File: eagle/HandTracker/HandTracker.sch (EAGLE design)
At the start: 9 parts, among them J1 ZX62-AB-5PA(31), U1 LSM9DS1TR, U2 MAX11629EEE+21-0055_E16+5_MXM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, U3 ATMEGA16U2-MU32M1-A_ATM-M

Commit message: continued making connections
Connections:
- new net CSA: U2.!CS
- new net CSAG: U1.CS_A/G
- new net CSM: U1.CS_M
- new net MISO: U$1.14, U1.SDO_A/G, U1.SDO_M, U2.DOUT
- new net MOSI: U$1.15, U1.SDA/SDI/SDO, U2.DIN
- new net SCLK: U$1.7, U1.SCL/SPC, U2.SCLK
- net GND: now also U1.GND, U1.GND_2, U1.RES, U1.RES_2, U1.RES_3, U1.RES_4, U1.RES_5, U2.GND
- net VCC: now also U1.VDD, U1.VDDIO, U1.VDDIO_2, U1.VDD_2, U2.REF, U2.VDD
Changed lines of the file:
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@@
 <part name="GND4" library="supply1" library_urn="urn:adsk.eagle:library:371" deviceset="GND" device=""/>
 <part name="P+3" library="supply1" library_urn="urn:adsk.eagle:library:371" deviceset="VCC" device=""/>
+<part name="P+4" library="supply1" library_urn="urn:adsk.eagle:library:371" deviceset="VCC" device=""/>
+<part name="GND5" library="supply1" library_urn="urn:adsk.eagle:library:371" deviceset="GND" device=""/>
+<part name="P+5" library="supply1" library_urn="urn:adsk.eagle:library:371" deviceset="VCC" device=""/>
+<part name="P+6" library="supply1" library_urn="urn:adsk.eagle:library:371" deviceset="VCC" device=""/>
+<part name="GND6" library="supply1" library_urn="urn:adsk.eagle:library:371" deviceset="GND" device=""/>
 </parts>
 <sheets>
@@
 <attribute name="VALUE" x="58.42" y="-53.34" size="1.778" layer="96" rot="R90"/>
 </instance>
+<instance part="P+4" gate="VCC" x="119.38" y="76.2" smashed="yes">
+<attribute name="VALUE" x="116.84" y="73.66" size="1.778" layer="96" rot="R90"/>
+</instance>
+<instance part="GND5" gate="1" x="119.38" y="58.42" smashed="yes">
+<attribute name="VALUE" x="116.84" y="55.88" size="1.778" layer="96"/>
+</instance>
+<instance part="P+5" gate="VCC" x="2.54" y="-25.4" smashed="yes">
+<attribute name="VALUE" x="0" y="-27.94" size="1.778" layer="96" rot="R90"/>
+</instance>
+<instance part="P+6" gate="VCC" x="-76.2" y="-27.94" smashed="yes">
+<attribute name="VALUE" x="-78.74" y="-30.48" size="1.778" layer="96" rot="R90"/>
+</instance>
+<instance part="GND6" gate="1" x="2.54" y="-60.96" smashed="yes">
+<attribute name="VALUE" x="0" y="-63.5" size="1.778" layer="96"/>
+</instance>
 </instances>
 <busses>
@@
 <wire x1="58.42" y1="-58.42" x2="58.42" y2="-73.66" width="0.1524" layer="91"/>
 <pinref part="GND4" gate="1" pin="GND"/>
+</segment>
+<segment>
+<pinref part="U2" gate="A" pin="GND"/>
+<wire x1="86.36" y1="66.04" x2="119.38" y2="66.04" width="0.1524" layer="91"/>
+<wire x1="119.38" y1="66.04" x2="119.38" y2="60.96" width="0.1524" layer="91"/>
+<pinref part="GND5" gate="1" pin="GND"/>
+</segment>
+<segment>
+<pinref part="U1" gate="A" pin="GND"/>
+<wire x1="-7.62" y1="-38.1" x2="2.54" y2="-38.1" width="0.1524" layer="91"/>
+<wire x1="2.54" y1="-38.1" x2="2.54" y2="-40.64" width="0.1524" layer="91"/>
+<pinref part="U1" gate="A" pin="GND_2"/>
+<wire x1="-7.62" y1="-40.64" x2="2.54" y2="-40.64" width="0.1524" layer="91"/>
+<junction x="2.54" y="-40.64"/>
+<pinref part="GND6" gate="1" pin="GND"/>
+<wire x1="2.54" y1="-40.64" x2="2.54" y2="-43.18" width="0.1524" layer="91"/>
+<pinref part="U1" gate="A" pin="RES_2"/>
+<wire x1="2.54" y1="-43.18" x2="2.54" y2="-45.72" width="0.1524" layer="91"/>
+<wire x1="2.54" y1="-45.72" x2="2.54" y2="-48.26" width="0.1524" layer="91"/>
+<wire x1="2.54" y1="-48.26" x2="2.54" y2="-50.8" width="0.1524" layer="91"/>
+<wire x1="2.54" y1="-50.8" x2="2.54" y2="-53.34" width="0.1524" layer="91"/>
+<wire x1="2.54" y1="-53.34" x2="2.54" y2="-58.42" width="0.1524" layer="91"/>
+<wire x1="-7.62" y1="-53.34" x2="2.54" y2="-53.34" width="0.1524" layer="91"/>
+<junction x="2.54" y="-53.34"/>
+<pinref part="U1" gate="A" pin="RES_3"/>
+<wire x1="-7.62" y1="-50.8" x2="2.54" y2="-50.8" width="0.1524" layer="91"/>
+<junction x="2.54" y="-50.8"/>
+<pinref part="U1" gate="A" pin="RES_4"/>
+<wire x1="-7.62" y1="-48.26" x2="2.54" y2="-48.26" width="0.1524" layer="91"/>
+<junction x="2.54" y="-48.26"/>
+<pinref part="U1" gate="A" pin="RES_5"/>
+<wire x1="-7.62" y1="-45.72" x2="2.54" y2="-45.72" width="0.1524" layer="91"/>
+<junction x="2.54" y="-45.72"/>
+<pinref part="U1" gate="A" pin="RES"/>
+<wire x1="-7.62" y1="-43.18" x2="2.54" y2="-43.18" width="0.1524" layer="91"/>
+<junction x="2.54" y="-43.18"/>
 </segment>
 </net>
@@
 <wire x1="60.96" y1="-60.96" x2="76.2" y2="-60.96" width="0.1524" layer="91"/>
 </segment>
+<segment>
+<pinref part="U2" gate="A" pin="VDD"/>
+<wire x1="86.36" y1="68.58" x2="93.98" y2="68.58" width="0.1524" layer="91"/>
+<wire x1="93.98" y1="68.58" x2="119.38" y2="68.58" width="0.1524" layer="91"/>
+<wire x1="119.38" y1="68.58" x2="119.38" y2="73.66" width="0.1524" layer="91"/>
+<wire x1="93.98" y1="68.58" x2="93.98" y2="63.5" width="0.1524" layer="91"/>
+<junction x="93.98" y="68.58"/>
+<pinref part="U2" gate="A" pin="REF"/>
+<wire x1="93.98" y1="63.5" x2="86.36" y2="63.5" width="0.1524" layer="91"/>
+<pinref part="P+4" gate="VCC" pin="VCC"/>
+</segment>
+<segment>
+<pinref part="U1" gate="A" pin="VDDIO"/>
+<wire x1="-63.5" y1="-33.02" x2="-71.12" y2="-33.02" width="0.1524" layer="91"/>
+<wire x1="-71.12" y1="-33.02" x2="-76.2" y2="-33.02" width="0.1524" layer="91"/>
+<wire x1="-76.2" y1="-33.02" x2="-76.2" y2="-30.48" width="0.1524" layer="91"/>
+<pinref part="P+6" gate="VCC" pin="VCC"/>
+<pinref part="U1" gate="A" pin="VDDIO_2"/>
+<wire x1="-63.5" y1="-27.94" x2="-71.12" y2="-27.94" width="0.1524" layer="91"/>
+<wire x1="-71.12" y1="-27.94" x2="-71.12" y2="-33.02" width="0.1524" layer="91"/>
+<junction x="-71.12" y="-33.02"/>
+</segment>
+<segment>
+<pinref part="U1" gate="A" pin="VDD_2"/>
+<wire x1="-7.62" y1="-33.02" x2="2.54" y2="-33.02" width="0.1524" layer="91"/>
+<pinref part="P+5" gate="VCC" pin="VCC"/>
+<wire x1="2.54" y1="-33.02" x2="2.54" y2="-30.48" width="0.1524" layer="91"/>
+<pinref part="U1" gate="A" pin="VDD"/>
+<wire x1="2.54" y1="-30.48" x2="2.54" y2="-27.94" width="0.1524" layer="91"/>
+<wire x1="-7.62" y1="-30.48" x2="2.54" y2="-30.48" width="0.1524" layer="91"/>
+<junction x="2.54" y="-30.48"/>
+</segment>
 </net>
 <net name="D-" class="0">
@@
 </segment>
 </net>
+<net name="SCLK" class="0">
+<segment>
+<pinref part="U$1" gate="G$1" pin="7"/>
+<wire x1="30.48" y1="-25.4" x2="27.94" y2="-25.4" width="0.1524" layer="91"/>
+<label x="25.4" y="-25.4" size="1.778" layer="95"/>
+</segment>
+<segment>
+<pinref part="U2" gate="A" pin="SCLK"/>
+<wire x1="86.36" y1="73.66" x2="88.9" y2="73.66" width="0.1524" layer="91"/>
+<label x="88.9" y="73.66" size="1.778" layer="95"/>
+</segment>
+<segment>
+<pinref part="U1" gate="A" pin="SCL/SPC"/>
+<wire x1="-63.5" y1="-30.48" x2="-66.04" y2="-30.48" width="0.1524" layer="91"/>
+<label x="-68.58" y="-30.48" size="1.778" layer="95"/>
+</segment>
+</net>
+<net name="MISO" class="0">
+<segment>
+<pinref part="U$1" gate="G$1" pin="14"/>
+<wire x1="78.74" y1="-25.4" x2="81.28" y2="-25.4" width="0.1524" layer="91"/>
+<label x="81.28" y="-25.4" size="1.778" layer="95"/>
+</segment>
+<segment>
+<pinref part="U2" gate="A" pin="DOUT"/>
+<wire x1="86.36" y1="78.74" x2="88.9" y2="78.74" width="0.1524" layer="91"/>
+<label x="88.9" y="78.74" size="1.778" layer="95"/>
+</segment>
+<segment>
+<pinref part="U1" gate="A" pin="SDO_M"/>
+<wire x1="-63.5" y1="-40.64" x2="-66.04" y2="-40.64" width="0.1524" layer="91"/>
+<label x="-68.58" y="-40.64" size="1.778" layer="95"/>
+</segment>
+<segment>
+<pinref part="U1" gate="A" pin="SDO_A/G"/>
+<wire x1="-63.5" y1="-38.1" x2="-66.04" y2="-38.1" width="0.1524" layer="91"/>
+<label x="-68.58" y="-38.1" size="1.778" layer="95"/>
+</segment>
+</net>
+<net name="MOSI" class="0">
+<segment>
+<pinref part="U$1" gate="G$1" pin="15"/>
+<wire x1="78.74" y1="-22.86" x2="81.28" y2="-22.86" width="0.1524" layer="91"/>
+<label x="81.28" y="-22.86" size="1.778" layer="95"/>
+</segment>
+<segment>
+<pinref part="U2" gate="A" pin="DIN"/>
+<wire x1="86.36" y1="76.2" x2="88.9" y2="76.2" width="0.1524" layer="91"/>
+<label x="88.9" y="76.2" size="1.778" layer="95"/>
+</segment>
+<segment>
+<pinref part="U1" gate="A" pin="SDA/SDI/SDO"/>
+<wire x1="-63.5" y1="-35.56" x2="-66.04" y2="-35.56" width="0.1524" layer="91"/>
+<label x="-68.58" y="-35.56" size="1.778" layer="95"/>
+</segment>
+</net>
+<net name="CSA" class="0">
+<segment>
+<pinref part="U2" gate="A" pin="!CS"/>
+<wire x1="86.36" y1="71.12" x2="88.9" y2="71.12" width="0.1524" layer="91"/>
+<label x="88.9" y="71.12" size="1.778" layer="95"/>
+</segment>
+</net>
+<net name="CSAG" class="0">
+<segment>
+<pinref part="U1" gate="A" pin="CS_A/G"/>
+<wire x1="-63.5" y1="-43.18" x2="-66.04" y2="-43.18" width="0.1524" layer="91"/>
+<label x="-68.58" y="-43.18" size="1.778" layer="95"/>
+</segment>
+</net>
+<net name="CSM" class="0">
+<segment>
+<pinref part="U1" gate="A" pin="CS_M"/>
+<wire x1="-63.5" y1="-45.72" x2="-66.04" y2="-45.72" width="0.1524" layer="91"/>
+<label x="-68.58" y="-45.72" size="1.778" layer="95"/>
+</segment>
+</net>

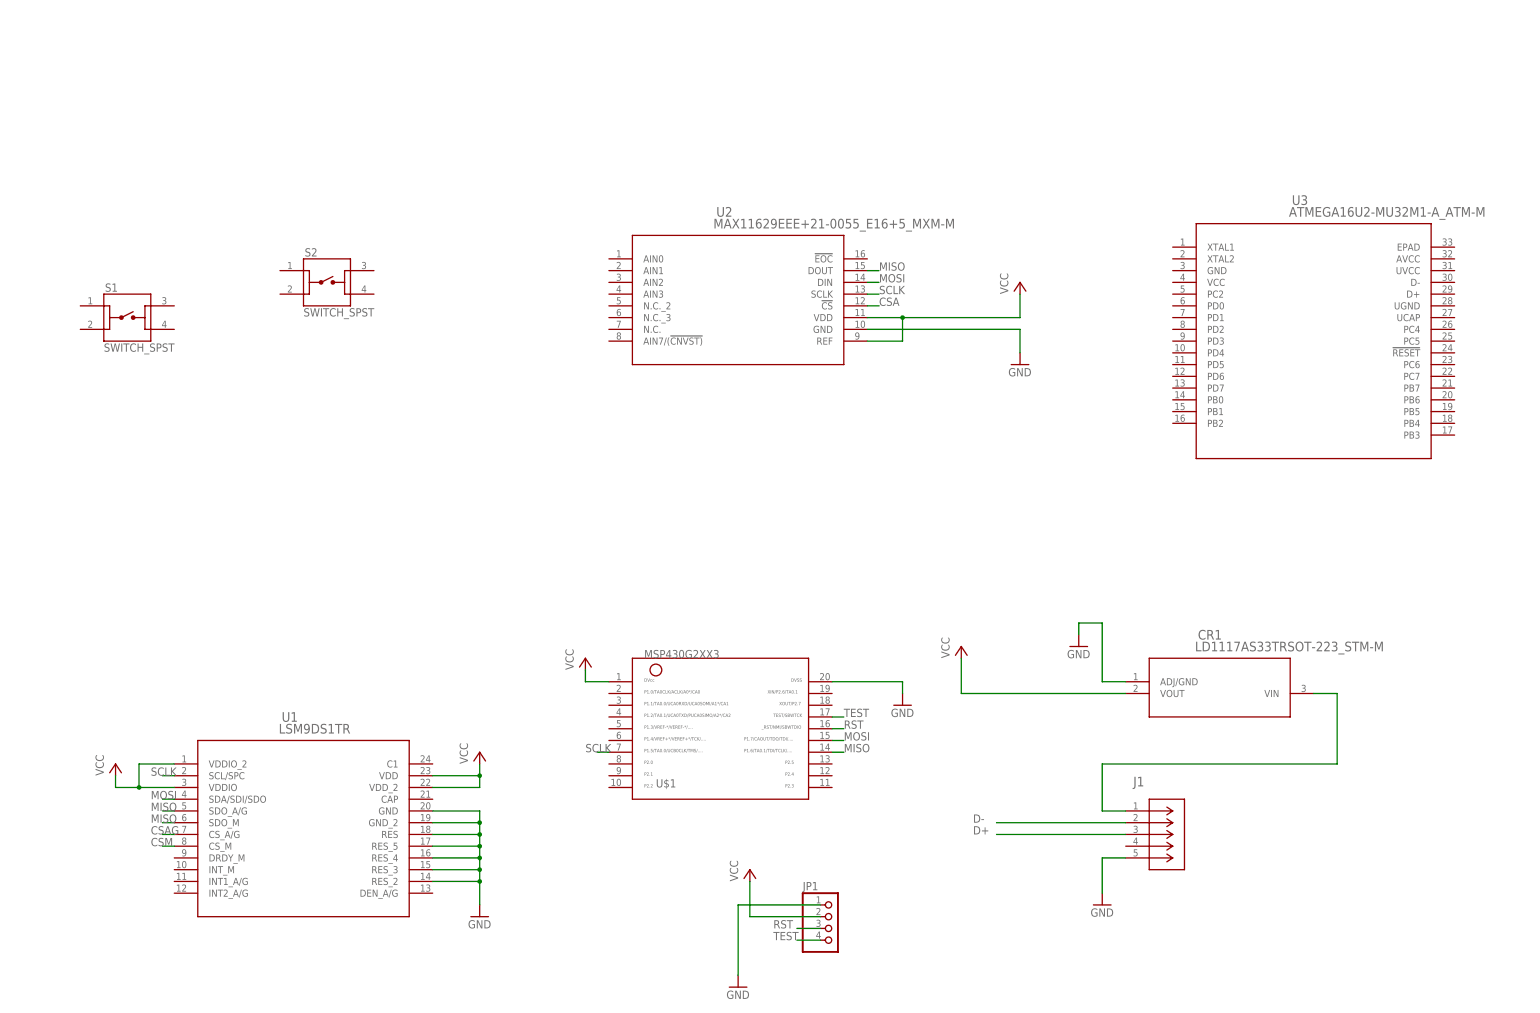
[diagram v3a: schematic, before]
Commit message: completed connections for all components except FT232
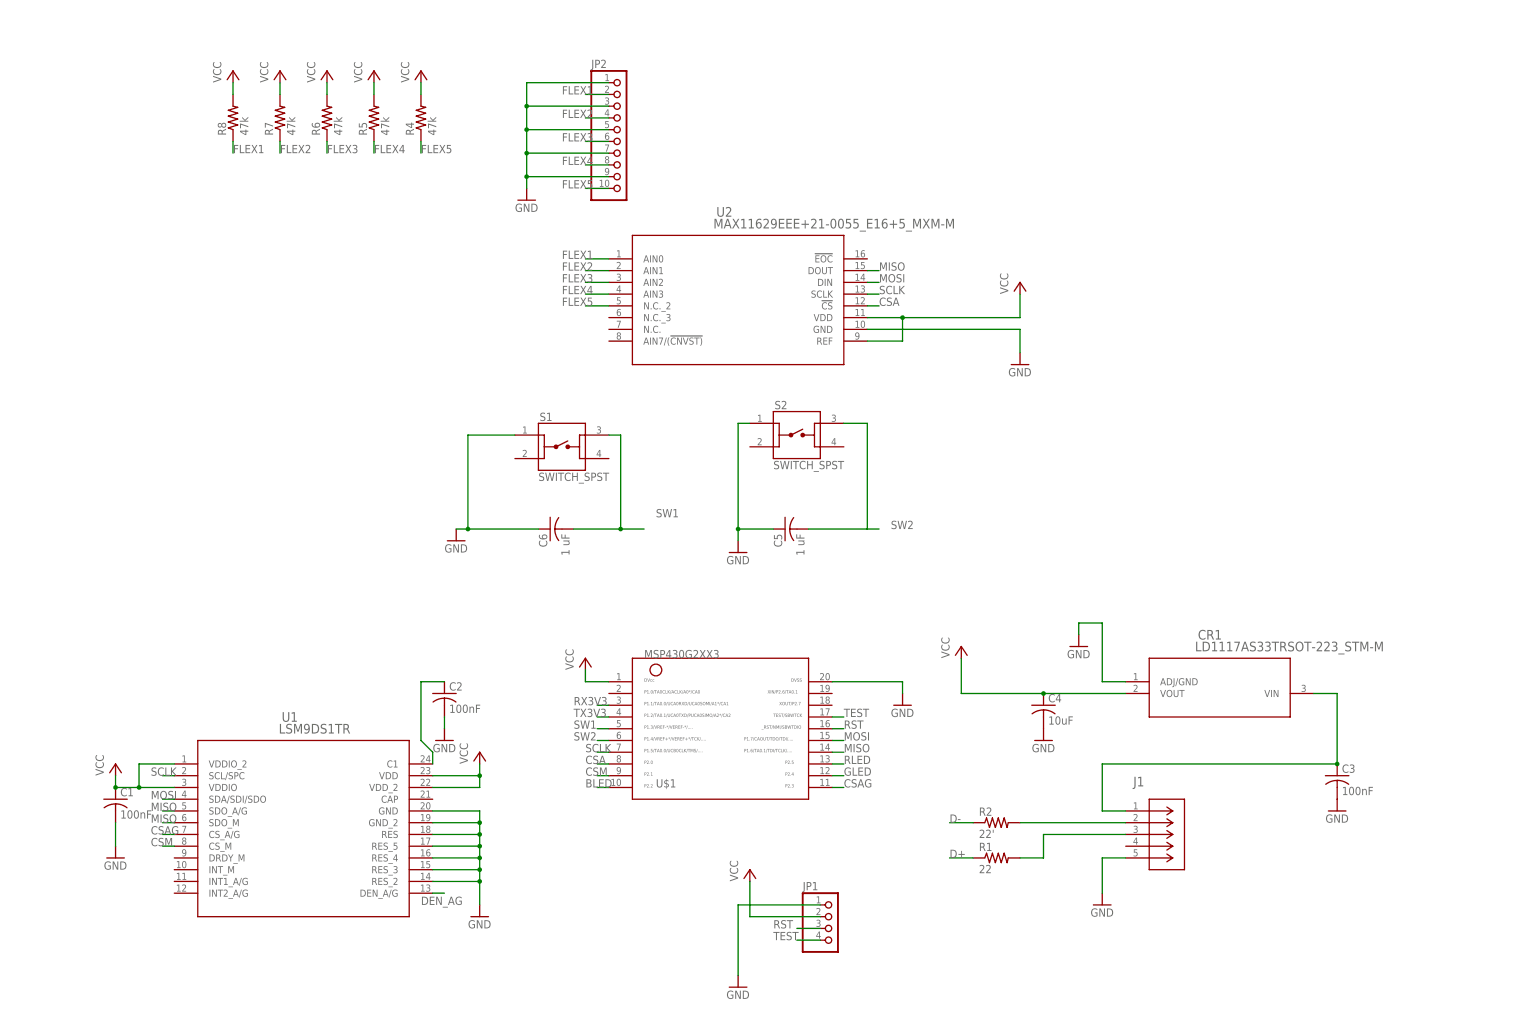
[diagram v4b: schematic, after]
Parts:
- removed U3: ATMEGA16U2-MU32M1-A_ATM-M, AtMega16U2-MU:ATMEGA16U2-MU32M1-A_ATM-M
- added C1, C2, C3: 100nF, rcl:C-USC1206
- added C4: 10uF, rcl:C-USC1206
- added C5, C6: 1 uF, rcl:C-USC1206
- added JP2: (no value), pinhead:PINHD-1X10
- added R1: 22, rcl:R-US_R1206
- added R2: 22', rcl:R-US_R1206
- added R4, R5, R6, R7, R8: 47k, rcl:R-US_R1206
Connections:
- new net BLED: U$1.10
- new net DEN_AG: U1.DEN_A/G
- new net FLEX1: JP2.2, R8.1, U2.AIN0
- new net FLEX2: JP2.4, R7.1, U2.AIN1
- new net FLEX3: JP2.6, R6.1, U2.AIN2
- new net FLEX4: JP2.8, R5.1, U2.AIN3
- new net FLEX5: JP2.10, R4.1, U2.N.C._2
- new net GLED: U$1.12
- new net N$1: C2.1, U1.C1
- new net N$2: J1.D+, R1.2
- new net N$5: J1.D-, R2.2
- new net RLED: U$1.13
- new net RX3V3: U$1.3
- new net SW1: C6.2, S1.3, U$1.5
- new net SW2: C5.2, S2.3, U$1.6
- new net TX3V3: U$1.4
- net CSA: now also U$1.8
- net CSAG: now also U$1.11
- net CSM: now also U$1.9
- net D+: now also R1.1; no longer J1.D+
- net D-: now also R2.1; no longer J1.D-
- net GND: now also C1.2, C2.2, C3.2, C4.2, C5.1, C6.1, JP2.1, JP2.3, JP2.5, JP2.7, JP2.9, S1.1, S2.1
- net N$3: now also C3.1
- net VCC: now also C1.1, C4.1, R4.2, R5.2, R6.2, R7.2, R8.2
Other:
- moved on the sheet: S1, S2
